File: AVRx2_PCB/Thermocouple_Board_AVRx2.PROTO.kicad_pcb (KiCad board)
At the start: 2 copper layers, 90 x 39 mm, 103 parts, among them J1 DAC_OUT, J2 SPI, J3 RST, J4 DAC, J5 UPDI-0, J6 UPDI-1, J7 EXP, Q1 DMN2310U, U1 AVR16EB, U10 MCP4726A0T-E/CH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

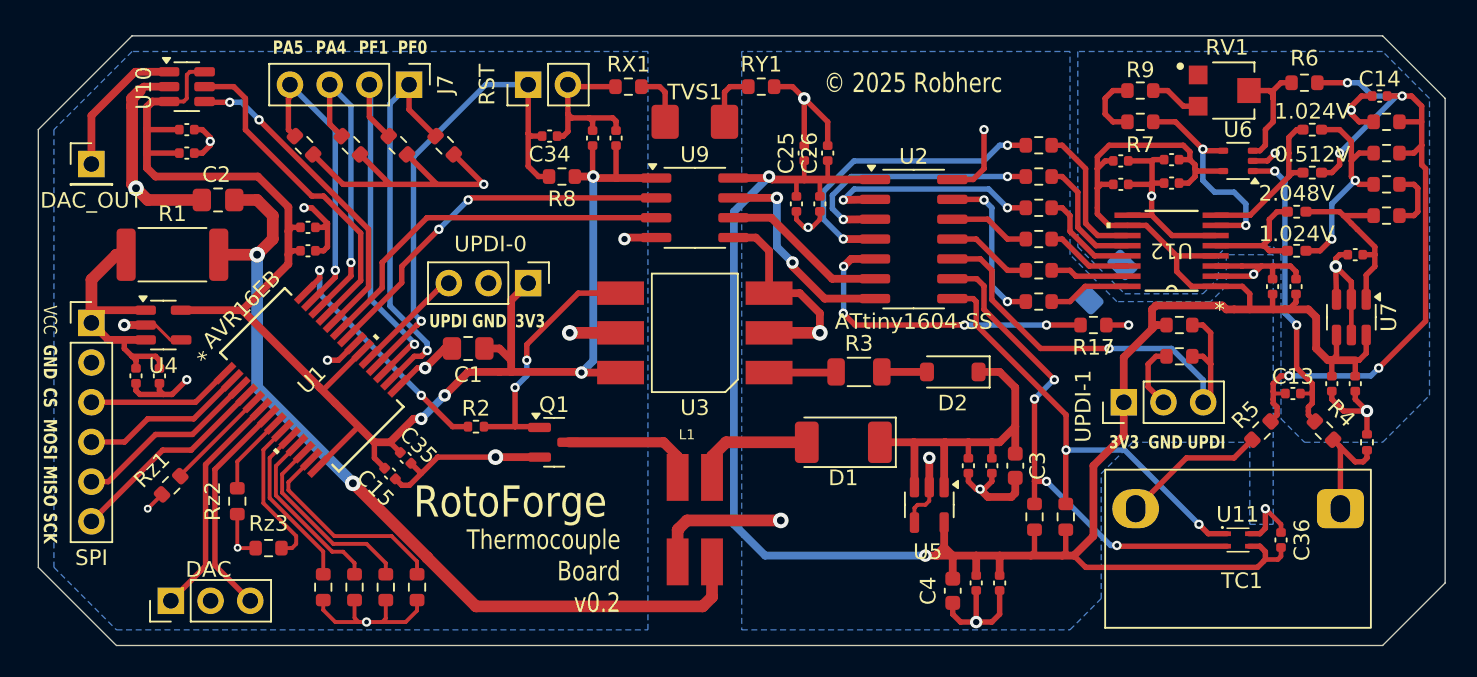
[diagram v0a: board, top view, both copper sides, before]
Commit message: Update pcb designs to further optimize layout, fix an error, and creat prototype layout with test points
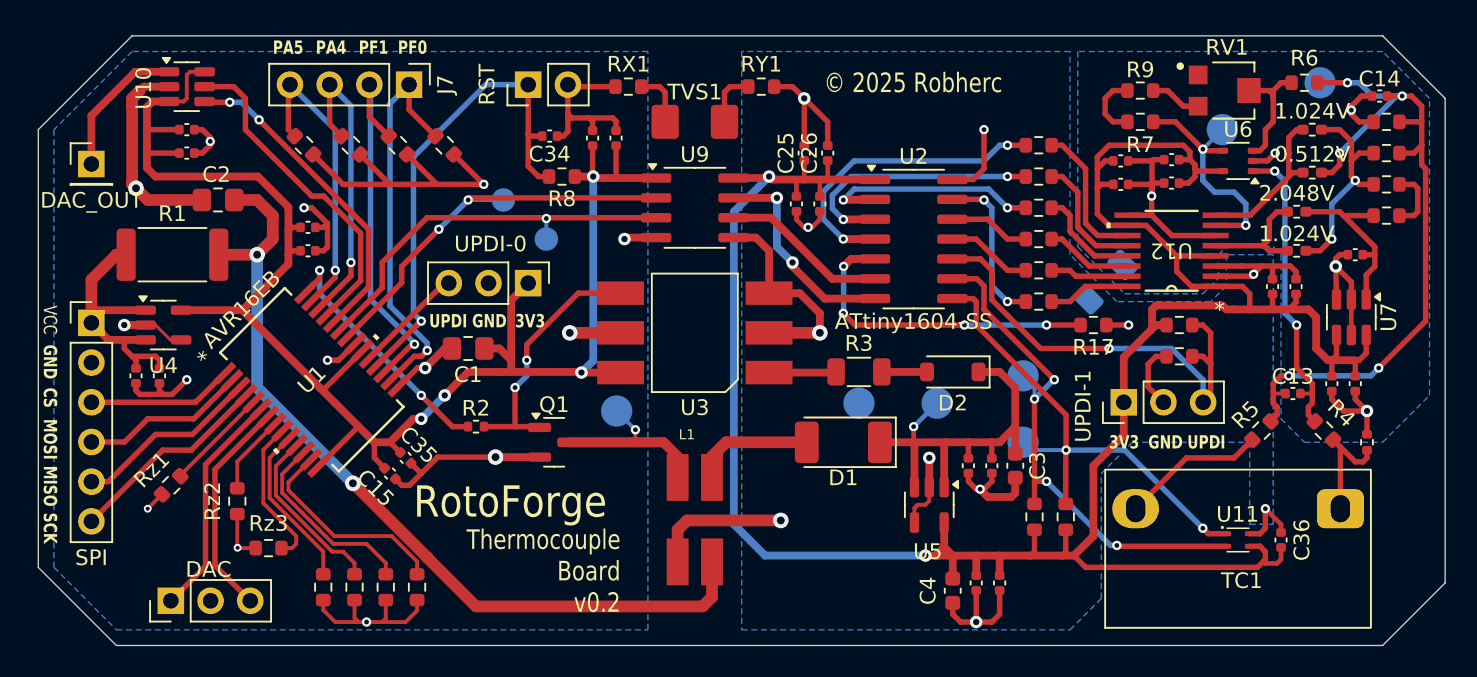
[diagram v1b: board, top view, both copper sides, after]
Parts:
- added 0.512V: TestPoint_Pad_D2.0mm, TestPoint:TestPoint_Pad_D2.0mm, B.Cu at (190.0, 81.0)
- added AIN+: TestPoint_Pad_D2.0mm, TestPoint:TestPoint_Pad_D2.0mm, B.Cu at (183.8, 84.0)
- added GND2: TestPoint_Pad_D2.0mm, TestPoint:TestPoint_Pad_D2.0mm, B.Cu at (160.5, 101.5)
- added RX: TestPoint_Pad_D1.5mm, TestPoint:TestPoint_Pad_D1.5mm, B.Cu at (140.5, 91.0)
- added SCL: TestPoint_Pad_D2.0mm, TestPoint:TestPoint_Pad_D2.0mm, B.Cu at (171.0, 99.8)
- added SDA: TestPoint_Pad_D2.0mm, TestPoint:TestPoint_Pad_D2.0mm, B.Cu at (171.0, 104.0)
- added SMPS: TestPoint_Pad_D2.0mm, TestPoint:TestPoint_Pad_D2.0mm, B.Cu at (145.0, 102.0)
- added TX: TestPoint_Pad_D1.5mm, TestPoint:TestPoint_Pad_D1.5mm, B.Cu at (137.8, 88.5)
- added VCC2: TestPoint_Pad_D2.0mm, TestPoint:TestPoint_Pad_D2.0mm, B.Cu at (165.5, 101.5)
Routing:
- net Net-(D1-K): track 23.9 -> 27.0 mm, vias 0 -> 1
- net SDA: track 29.5 -> 32.4 mm
- net Net-(Q1-D): track 8.69 -> 11.2 mm, vias 0 -> 1
- net ISO-TX: track 24.0 -> 26.2 mm
- net SCL: track 32.6 -> 34.4 mm
- net Net-(U12-AINP): track 13.9 -> 15.7 mm
- net Net-(C13-Pad2): track 47.4 -> 49.1 mm
- net ISO-RX: track 24.0 -> 25.4 mm, vias 0 -> 1

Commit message: Fix a couple of switched traces
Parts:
- L1: value 22uH -> SRF0703-6R8M
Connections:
- U1 pad 1: /Output MCU/CS -> Net-(U1-PC3)
- U1 pad 5: Net-(U1-PC3) -> /Output MCU/CS
- U9 pad 6: Net-(U2-PB3) -> Net-(U2-PB2)
- U9 pad 7: Net-(U2-PB2) -> Net-(U2-PB3)
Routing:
- net /Output MCU/CS: track 9.31 -> 15.3 mm, vias 0 -> 1
- net Net-(U2-PB2): track 13.7 -> 11.6 mm, vias 2 -> 0
- net Net-(U1-PC3): track 6.69 -> 7.75 mm, vias 0 -> 3
- net Net-(U2-PB3): track 10.7 -> 11.2 mm

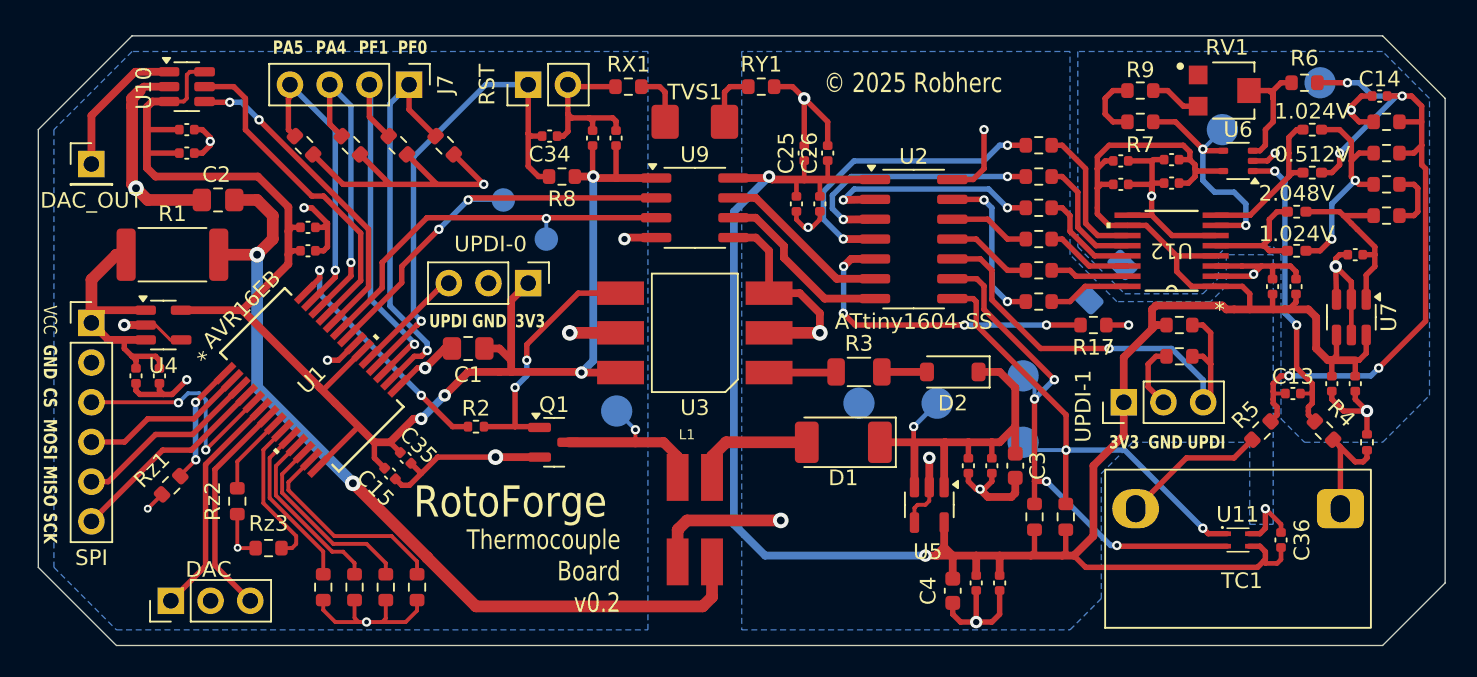
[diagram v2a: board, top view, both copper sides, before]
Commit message: Fix crossed traces that were found during prototype testing
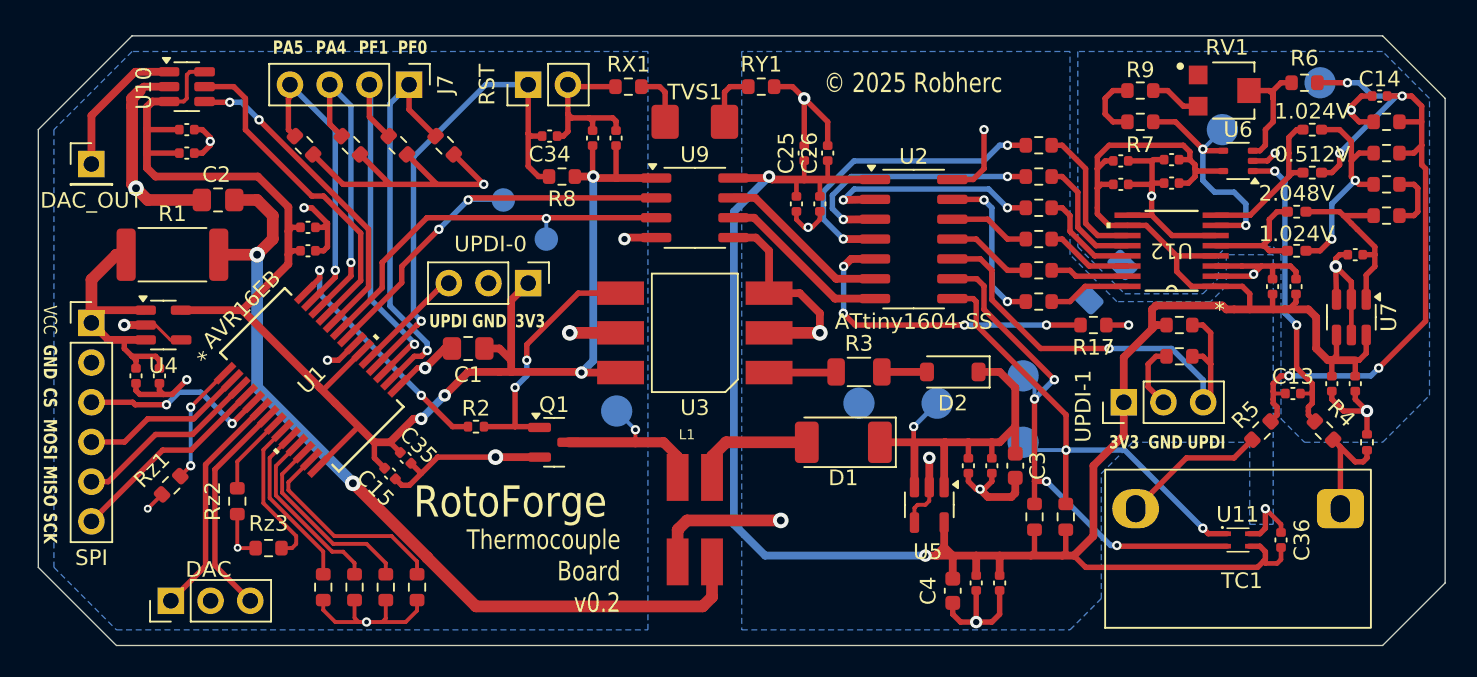
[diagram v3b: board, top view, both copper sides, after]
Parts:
- L1: value SRF0703-6R8M -> 22uH
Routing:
- net /Output MCU/CS: track 15.3 -> 12.2 mm, vias 1 -> 2
- net Net-(U1-PC3): track 7.75 -> 7.84 mm, vias 3 -> 2

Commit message: update to latest kicad version
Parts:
- L1: value 22uH -> SRF0703-6R8M
